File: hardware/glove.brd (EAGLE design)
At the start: 50.8 x 36.8 mm, 90 parts, among them J1 TC2030-JLINK-NL, J2 MICRO_USB_B_JST_MC5BR3-M404-4S, P1 DMP1045U, T0 WIREPAD1,6/0,8, T1 WIREPAD1,6/0,8, T2 WIREPAD1,6/0,8, T3 WIREPAD1,6/0,8, U1 NRF51822QF, U2 BNO055, U3 AT42QT1070, U4 MCP73831, U5 LP3855EMP-ADJ, X1 ABS05-32.768KHZ-9-T

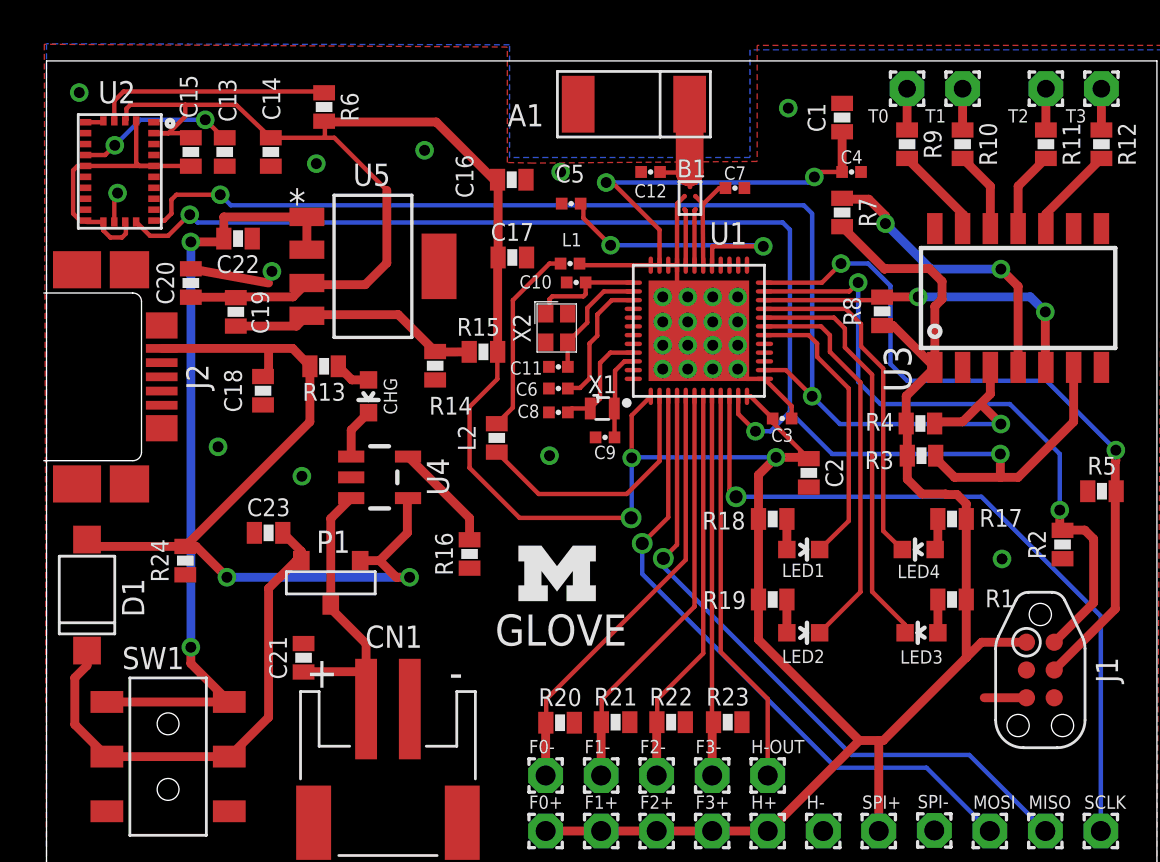
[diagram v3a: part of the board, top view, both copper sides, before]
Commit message: Moved some parts slightly and ADDED PWR LED
Possible issues with bus routing
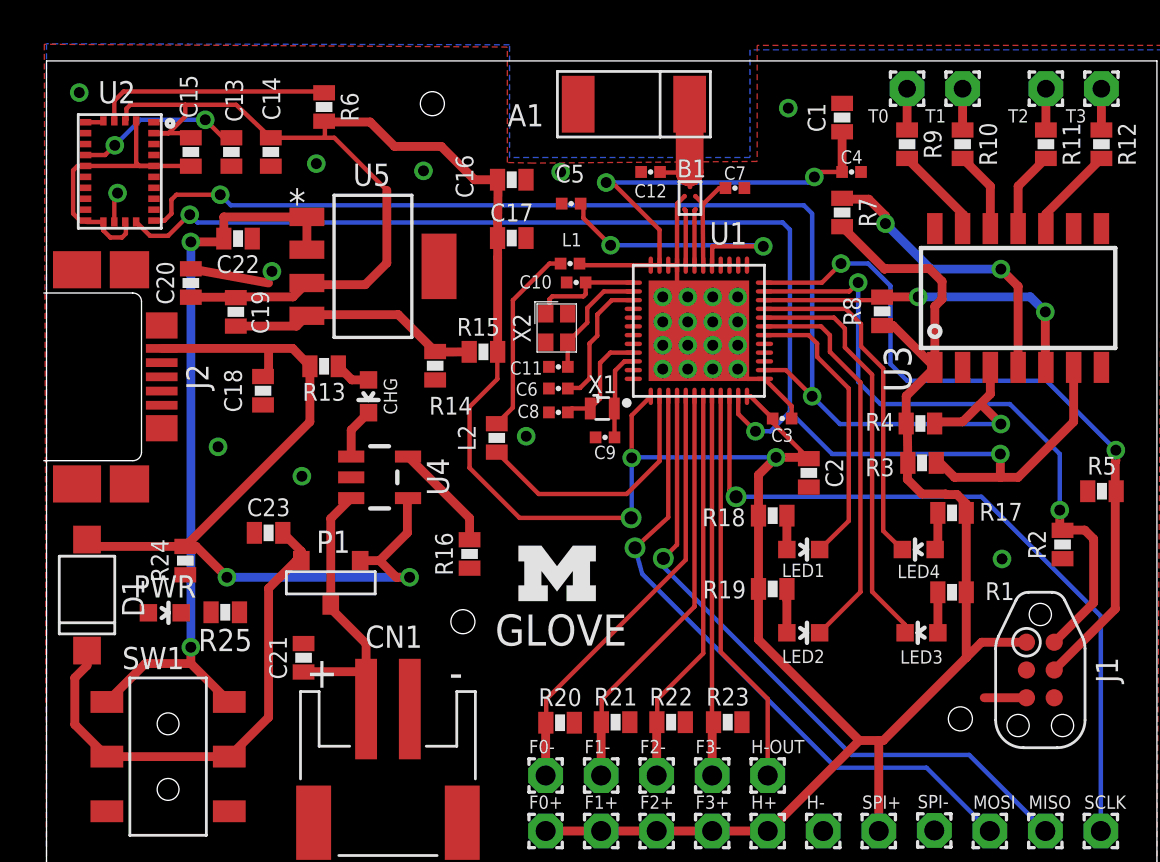
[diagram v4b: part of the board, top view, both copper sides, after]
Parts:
- added PWR: LED0603, leds:LED-0603
- added R25: 470, passives:0603-RES
- moved C17 0.89 mm to (21.3, 23.6)
- moved R19 0.48 mm to (33.2, 7.59)
- moved R3 0.33 mm to (40.1, 13.4)
- moved R1 0.33 mm to (41.4, 7.44)
- moved C13 0.30 mm to (8.46, 27.6)
- moved R17 0.28 mm to (41.4, 11.1)
- moved R18 0.15 mm to (33.2, 10.9)
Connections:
- new net N$17: PWR.C, R25.2
- net GND: now also R25.1
- net N$5: now also PWR.A
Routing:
- net N$5: track 35.5 -> 34.4 mm

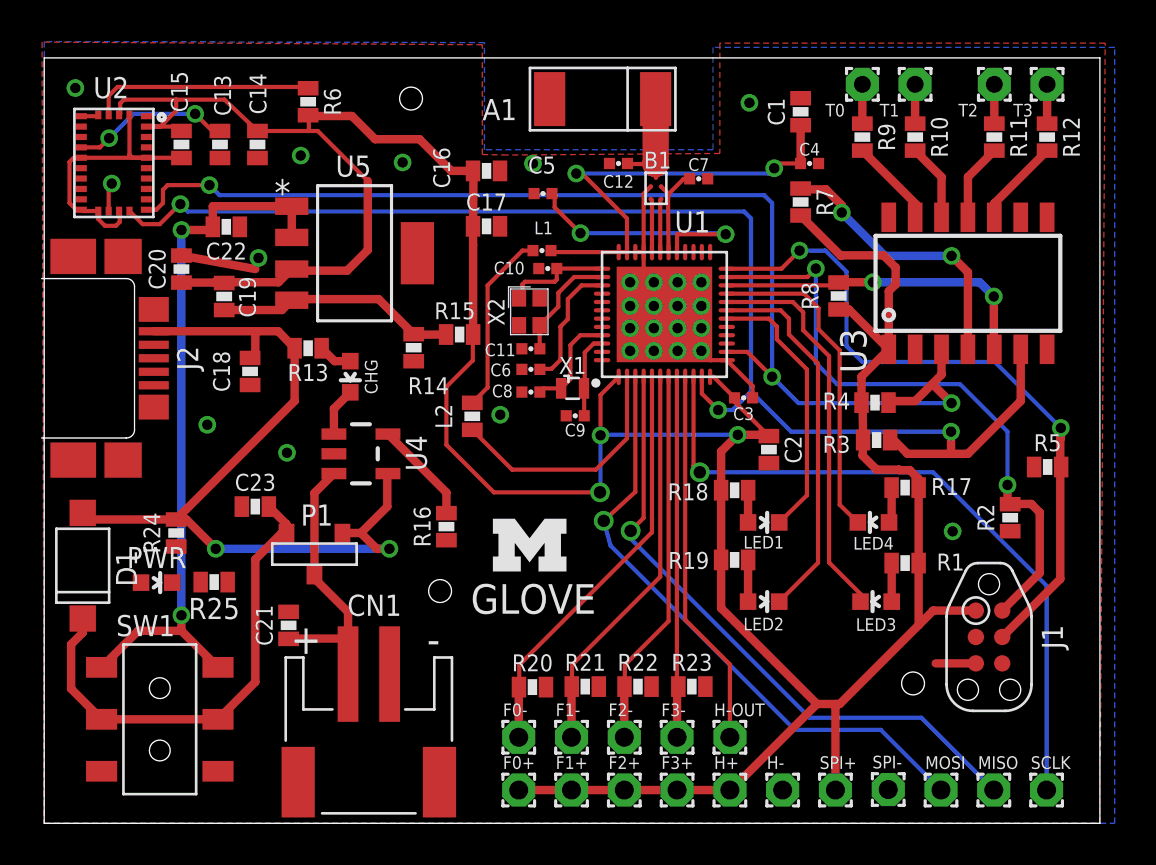
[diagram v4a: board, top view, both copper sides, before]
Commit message: Renamed Parts/Updated BOM
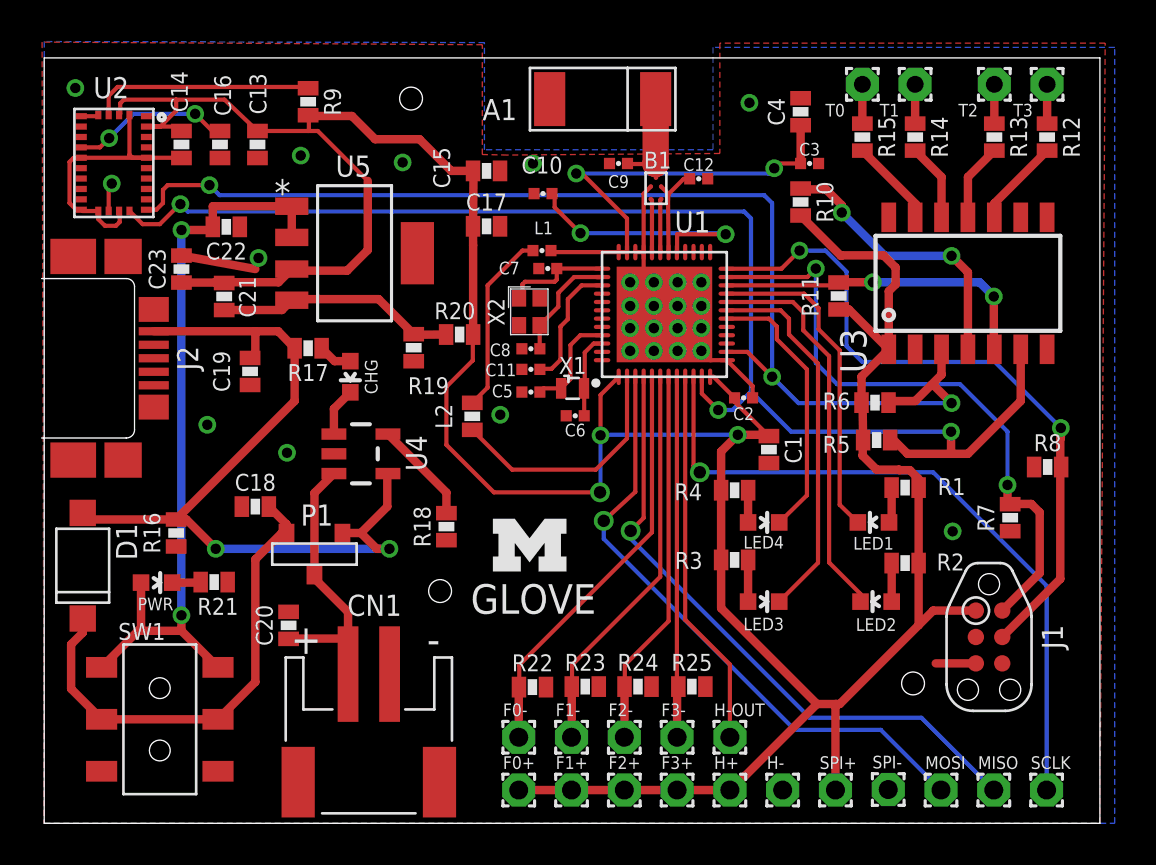
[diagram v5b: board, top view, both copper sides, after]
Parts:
- C1: value 1.0 uF -> 4.7 uF
- C10: value 12 pF -> 47 nF
- C11: value 12 pF -> 1.0 nF
- C12: value 0.8 pF -> 2.2 nF
- C13: value 100 nF -> 6.8 nF
- C14: value 6.8 nF -> 120 nF
- C15: value 120 nF -> 100 nF
- C18: value 4.7 uF -> 1uF
- C19: value 8 nF -> 4.7 uF
- C2: value 4.7 uF -> 100 nF; device passives:0603_CAP -> passives:0402_CAP
- C20: value 10 uF -> 4.7 uF
- C21: value 4.7 uF -> 8 nF
- C23: value 1uF -> 10 uF
- C3: value 100 nF -> 1.0 nF
- C4: value 1.0 nF -> 1.0 uF; device passives:0402_CAP -> passives:0603_CAP
- C5: value 47 nF -> 12 pF
- C6: value 1.0 nF -> 12 pF
- C7: value 2.2 nF -> 12 pF
- C9: value 12 pF -> 0.8 pF
- R10, R11: value 10 k -> 47 k
- R13: value 470 -> 10 k
- R14: value 250 -> 10 k
- R15: value 440 -> 10 k
- R16: value 2 k -> 100k
- R17: value 1 k -> 470
- R18: value 1 k -> 2 k
- R19: value 1 k -> 250
- R2: value 150 -> 1 k
- R20: value (none) -> 440
- R21: value (none) -> 470
- R24: value 100k -> (none)
- R25: value 470 -> (none)
- R5: value 12 k -> 1 k
- R6: value 10 k -> 1 k
- R7: value 47 k -> 150
- R8: value 47 k -> 12 k
- moved R13 34.5 mm to (45.7, 27.9), turned to 270 degrees
- moved R6 30.9 mm to (40.0, 15.2), turned to 180 degrees
- moved R17 29.5 mm to (12.7, 17.8), turned to 180 degrees
- moved R9 26.7 mm to (12.7, 29.6)
- moved R14 26.2 mm to (41.9, 27.9)
- moved R25 23.5 mm to (31.2, 1.50), turned to 0 degrees
- moved R24 23.4 mm to (28.6, 1.50), turned to 0 degrees
- moved R15 21.6 mm to (39.4, 27.9), turned to 270 degrees
- moved R21 18.6 mm to (8.18, 6.53), turned to 180 degrees
- moved R19 18.5 mm to (17.8, 17.8), turned to 270 degrees
- moved R7 18.2 mm to (46.5, 9.63), turned to 90 degrees
- moved C20 17.9 mm to (11.8, 4.45)
- moved R20 17.3 mm to (20.0, 18.4), turned to 180 degrees
- moved C1 16.3 mm to (34.9, 12.9), turned to 270 degrees
- moved C21 16.1 mm to (8.66, 20.3)
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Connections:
- net !CHANGE: now also R11.1; no longer R8.1
- net FLEX0: now also R22.1; no longer R20.1
- net FLEX1: now also R23.1; no longer R21.1
- net FLEX2: now also R24.1; no longer R22.1
- net FLEX3: now also R25.1; no longer R23.1
- net GND: now also C18.1, C19.2, C23.2, R18.1, R19.2, R21.1, R24.2, R25.2, R7.1, R8.1; no longer C18.2, C21.2, C23.1, R14.2, R2.1, R20.2, R21.2, R24.1, R25.1, R5.1
- net N$1: now also C18.2; no longer C23.2
- net N$10: now also LED1.C; no longer LED4.C
- net N$11: now also LED1.A, R1.1; no longer LED4.A, R17.1
- net N$12: now also LED4.C; no longer LED1.C
- net N$13: now also LED4.A, R4.1; no longer LED1.A, R18.1
- net N$16: now also C3.1; no longer C1.1
- net N$17: now also R21.2; no longer R25.2
- net N$18: now also R9.1; no longer R6.1
- net N$19: now also R7.2; no longer R2.2
- net N$2: now also R17.1; no longer R13.1
- net N$20: now also C8.1; no longer C11.1
- net N$23: now also C12.1; no longer C7.1
- net N$24: now also C9.1; no longer C12.1
- net N$25: now also C10.1; no longer C5.1
- net N$26: now also C11.1; no longer C6.1
- net N$27: now also C5.1; no longer C8.1
- net N$28: now also C6.1; no longer C9.1
- net N$29: now also C7.1; no longer C10.1
- net N$30: now also R8.2; no longer R5.2
- net N$33: now also R13.2; no longer R11.2
- net N$34: now also R13.1; no longer R11.1
- net N$35: now also R14.2; no longer R10.2
- net N$36: now also R14.1; no longer R10.1
- net N$37: now also R15.2; no longer R9.2
- net N$38: now also C19.1, R16.2, R17.2; no longer C18.1, R13.2, R24.2
- net N$39: now also R15.1; no longer R9.1
- net N$4: now also R18.2; no longer R16.2
- net N$40: now also R10.1; no longer R7.1
- net N$41: now also C20.1; no longer C21.1
- net N$42: now also LED3.A, R3.1; no longer LED2.A, R19.1
- net N$43: now also LED3.C; no longer LED2.C
- net N$6: now also LED2.C; no longer LED3.C
- net N$7: now also C21.1, R19.1, R20.2; no longer C19.1, R14.1, R15.2
- net N$8: now also LED2.A, R2.1; no longer LED3.A, R1.1
- net N$9: now also C16.1; no longer C13.1
- net SCL: now also R5.1; no longer R3.1
- net SDA: now also R6.1; no longer R4.1
- net VCC: now also C1.1, C13.1, C21.2, C23.1, R10.2, R11.2, R2.2, R20.1, R5.2, R9.2; no longer C16.1, C19.2, C20.1, C3.1, R15.1, R17.2, R18.2, R19.2, R7.2, R8.2
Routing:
- net N$5: track 34.4 -> 36.8 mm
- net N$17: track 0.00 -> 1.38 mm

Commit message: The board is done...hopefully
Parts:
- removed MISO: WIREPAD1,6/0,9, wirepad:1,6/0,9
- R21: value 470 -> 250
- R22, R23, R24, R25: value (none) -> 20k
- moved PWR 21.0 mm to (26.3, 8.53), turned to 180 degrees
- moved R21 13.5 mm to (21.3, 3.48), turned to 90 degrees
- moved SPI+ 2.57 mm to (40.6, -3.40)
- moved MOSI 2.54 mm to (45.7, -3.48)
- moved SPI- 2.54 mm to (43.2, -3.45)
- moved C5 1.27 mm to (23.4, 14.4), turned to 270 degrees
- moved U$1 0.70 mm to (20.9, 7.26)
- moved C6 0.58 mm to (25.3, 14.0)
- moved C11 0.33 mm to (23.3, 16.5)
- moved C8 0.18 mm to (23.4, 17.6)
- moved R6 0.14 mm to (40.1, 15.3), turned to 0 degrees
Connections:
- removed net MISO: MISO.1, U1.4
- removed net N$5: C22.2, PWR.A, SW1.O1, SW1.O2, U5.1, U5.2
- new net N$54: C22.2, SW1.O1, SW1.O2, U5.1, U5.2
- net MOSI: now also U1.25; no longer U1.3
- net SCLK: now also U1.26; no longer U1.10
- net SDA: now also R6.2, U1.3; no longer R6.1, U1.14
- net VCC: now also PWR.A, R6.1; no longer R6.2
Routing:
- net N$5: track 36.8 -> 0.00 mm, vias 2 -> 0
- net N$54: track 0.00 -> 34.6 mm, vias 0 -> 2
- net MISO: track 30.5 -> 0.00 mm, vias 1 -> 0
- net MOSI: track 29.7 -> 51.4 mm
- net SDA: track 57.2 -> 78.4 mm
- net SCLK: track 33.5 -> 54.3 mm, vias 1 -> 2
- net N$17: track 1.38 -> 6.46 mm
- net N$25: track 12.8 -> 9.45 mm
- net VCC: track 156.2 -> 158.6 mm
- net N$27: track 5.08 -> 6.31 mm
- net N$28: track 4.08 -> 4.71 mm
